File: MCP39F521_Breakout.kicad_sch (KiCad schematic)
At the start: 37 parts, among them J11 Conn_01x10, J2 Conn_01x01, J4 Conn_01x01, J5 Conn_01x01, U1 MCP39F521, U2 MCP9700AT-ETT, Y1 Crystal

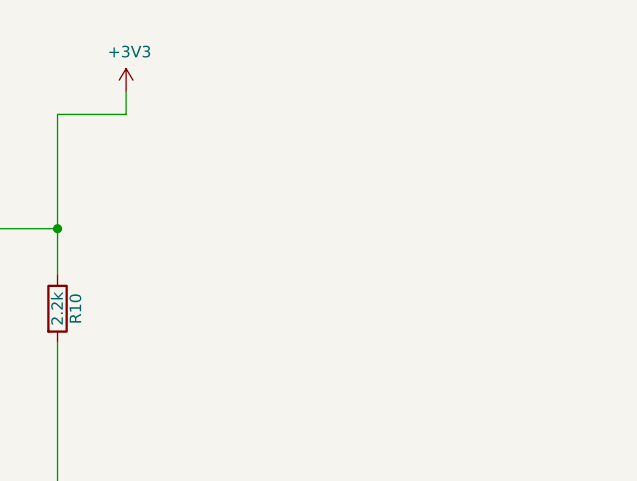
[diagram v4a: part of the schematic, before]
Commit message: Clean up silk screen
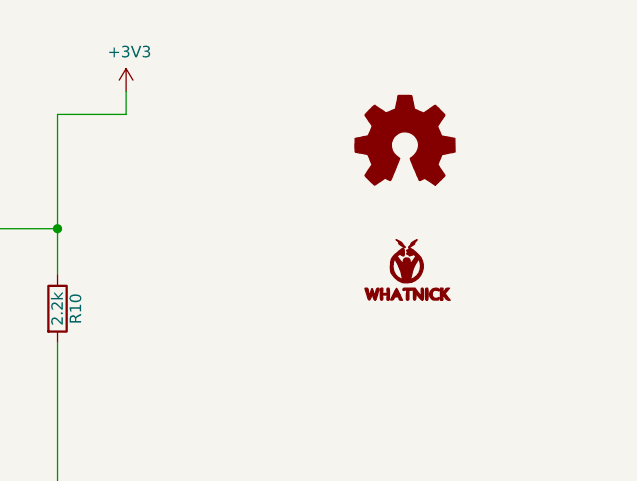
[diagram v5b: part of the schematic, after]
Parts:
- added LOGO1: Logo_Open_Hardware_Small, Symbol:OSHW-Logo2_7.3x6mm_SilkScreen, symbol Graphic:Logo_Open_Hardware_Small
- added LOGO2: LOGO, Whatnick_logo:Whatnick_logo, symbol whatnick:LOGO
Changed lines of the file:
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@@
+    )
+  )
+  (symbol (lib_id "whatnick:LOGO") (at 249.8344 59.182 0) (unit 1)
+    (in_bom yes) (on_board yes)
+    (property "Reference" "LOGO2" (id 0) (at 249.8344 61.7728 0)
+      (effects (font (size 1.524 1.524)) hide)
+    )
+    (property "Value" "LOGO" (id 1) (at 249.8344 56.5912 0)
+      (effects (font (size 1.524 1.524)) hide)
+    )
+    (property "Footprint" "Whatnick_logo:Whatnick_logo" (id 2) (at 249.8344 59.182 0)
+      (effects (font (size 1.27 1.27)) hide)
+    )
+    (property "Datasheet" "" (id 3) (at 249.8344 59.182 0)
+      (effects (font (size 1.27 1.27)) hide)
+    )
+    (property "DNP" "..." (id 4) (at 249.8344 59.182 0)
+      (effects (font (size 1.27 1.27)) hide)
+    )
+  )
+  (symbol (lib_id "Graphic:Logo_Open_Hardware_Small") (at 249.5804 45.4152 0) (unit 1)
+    (in_bom yes) (on_board yes)
+    (property "Reference" "LOGO1" (id 0) (at 249.5804 38.4302 0)
+      (effects (font (size 1.27 1.27)) hide)
+    )
+    (property "Value" "Logo_Open_Hardware_Small" (id 1) (at 249.5804 51.1302 0)
+      (effects (font (size 1.27 1.27)) hide)
+    )
+    (property "Footprint" "Symbol:OSHW-Logo2_7.3x6mm_SilkScreen" (id 2) (at 249.5804 45.4152 0)
+      (effects (font (size 1.27 1.27)) hide)
+    )
+    (property "Datasheet" "~" (id 3) (at 249.5804 45.4152 0)
+      (effects (font (size 1.27 1.27)) hide)
+    )
+    (property "DNP" "..." (id 4) (at 249.5804 45.4152 0)
+      (effects (font (size 1.27 1.27)) hide)
     )
   )
@@
       (reference "L2") (unit 1) (value "FB 300ohm") (footprint "Inductor_SMD:L_0603_1608Metric")
     )
+    (path "/ebd4b0ad-a9ba-4337-bd8b-dba09d2c6b78"
+      (reference "LOGO1") (unit 1) (value "Logo_Open_Hardware_Small") (footprint "Symbol:OSHW-Logo2_7.3x6mm_SilkScreen")
+    )
+    (path "/371039ab-54b3-4110-96fc-8866fad4e8dd"
+      (reference "LOGO2") (unit 1) (value "LOGO") (footprint "Whatnick_logo:Whatnick_logo")
+    )
     (path "/2342108e-64ef-42af-a750-f275372ffd41"

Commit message: Create gerbers and swap to non-via footprint
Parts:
- U1: footprint Package_DFN_QFN:QFN-28-1EP_5x5mm_P0.5mm_EP3.35x3.35mm_ThermalVias -> Package_DFN_QFN:QFN-28-1EP_5x5mm_P0.5mm_EP3.35x3.35mm
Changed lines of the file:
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@@
       (effects (font (size 1.524 1.524)))
     )
-    (property "Footprint" "Package_DFN_QFN:QFN-28-1EP_5x5mm_P0.5mm_EP3.35x3.35mm_ThermalVias" (id 2) (at 153.8224 74.93 0)
+    (property "Footprint" "Package_DFN_QFN:QFN-28-1EP_5x5mm_P0.5mm_EP3.35x3.35mm" (id 2) (at 153.8224 74.93 0)
       (effects (font (size 1.524 1.524)) hide)
     )
@@
     )
     (path "/da78d0ed-192f-4411-a0f9-79bdfc0c146d"
-      (reference "U1") (unit 1) (value "MCP39F521") (footprint "Package_DFN_QFN:QFN-28-1EP_5x5mm_P0.5mm_EP3.35x3.35mm_ThermalVias")
+      (reference "U1") (unit 1) (value "MCP39F521") (footprint "Package_DFN_QFN:QFN-28-1EP_5x5mm_P0.5mm_EP3.35x3.35mm")
     )
     (path "/3119c087-44b1-40ae-b65a-35145a036b16"

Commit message: Updated BOM
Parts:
- A0, A1, J2, J4, J5, TP1, TP2, TP3: DNP (none) -> ...
- C1, C2, C3, C4: manf# (none) -> 0603YC333KAT2A
- C10, C9: manf# (none) -> C0603C220K4GACTU
- C11, C5, C8: manf# (none) -> C0603C104K4PACTU
- C6, C7: manf# (none) -> CL21A225KAFNNNE
- L1, L2: manf# (none) -> NFZ2MSD301SZ10L
- R1, R2, R3, R4: manf# (none) -> CR0603-FX-1501ELF
- R10, R9: manf# (none) -> CR0603-JW-222ELF
- R11, R12: manf# (none) -> CRL0603-FW-2R40ELF
- R5, R8: manf# (none) -> CR0603-JW-472ELF
- R6: manf# (none) -> CR0603AJ/-000EAS
- R7: manf# (none) -> CR0603-FX-10R0ELF
- U1: manf# (none) -> MCP39F521-E/MQ
- U2: manf# (none) -> MCP9700T-E/TT
- Y1: manf# (none) -> LFXTAL003071Reel
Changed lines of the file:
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@@
+      (effects (font (size 1.27 1.27)) hide)
+    )
+    (property "DNP" "..." (id 4) (at 101.7524 54.61 0)
       (effects (font (size 1.27 1.27)) hide)
     )
@@
       (effects (font (size 1.27 1.27)) hide)
     )
+    (property "DNP" "..." (id 4) (at 136.0424 39.37 0)
+      (effects (font (size 1.27 1.27)) hide)
+    )
   )
   (symbol (lib_id "Connector:TestPoint") (at 160.1724 39.37 0) (unit 1)
@@
       (effects (font (size 1.27 1.27)) hide)
     )
+    (property "DNP" "..." (id 4) (at 160.1724 39.37 0)
+      (effects (font (size 1.27 1.27)) hide)
+    )
   )
   (symbol (lib_id "power:+3.3VA") (at 78.1812 131.7244 0) (unit 1)
@@
       (effects (font (size 1.27 1.27)) hide)
     )
+    (property "manf#" "CR0603-FX-1501ELF" (id 4) (at 76.3524 168.91 0)
+      (effects (font (size 1.27 1.27)) hide)
+    )
   )
   (symbol (lib_id "Device:R") (at 76.3524 180.34 0) (unit 1)
@@
       (effects (font (size 1.27 1.27)) hide)
     )
+    (property "manf#" "CR0603-FX-1501ELF" (id 4) (at 76.3524 180.34 0)
+      (effects (font (size 1.27 1.27)) hide)
+    )
   )
   (symbol (lib_id "Device:R") (at 77.978 113.9952 0) (unit 1)
@@
       (effects (font (size 1.27 1.27)) hide)
     )
+    (property "manf#" "CRL0603-FW-2R40ELF" (id 4) (at 77.978 113.9952 0)
+      (effects (font (size 1.27 1.27)) hide)
+    )
   )
   (symbol (lib_id "Device:R") (at 78.0288 94.3356 0) (unit 1)
@@
       (effects (font (size 1.27 1.27)) hide)
     )
+    (property "manf#" "CRL0603-FW-2R40ELF" (id 4) (at 78.0288 94.3356 0)
+      (effects (font (size 1.27 1.27)) hide)
+    )
   )
   (symbol (lib_id "Device:R") (at 104.2924 99.06 270) (unit 1)
@@
       (effects (font (size 1.27 1.27)) hide)
     )
+    (property "manf#" "CR0603-FX-1501ELF" (id 4) (at 104.2924 99.06 0)
+      (effects (font (size 1.27 1.27)) hide)
+    )
   )
   (symbol (lib_id "Device:R") (at 104.2924 109.22 270) (unit 1)
@@
       (effects (font (size 1.27 1.27)) hide)
     )
+    (property "manf#" "CR0603-FX-1501ELF" (id 4) (at 104.2924 109.22 0)
+      (effects (font (size 1.27 1.27)) hide)
+    )
   )
   (symbol (lib_id "Device:R") (at 109.3724 68.58 0) (unit 1)
@@
       (effects (font (size 1.27 1.27)) hide)
     )
+    (property "manf#" "CR0603-JW-472ELF" (id 4) (at 109.3724 68.58 0)
+      (effects (font (size 1.27 1.27)) hide)
+    )
   )
   (symbol (lib_id "Device:R") (at 147.4724 39.37 270) (unit 1)
@@
       (effects (font (size 1.27 1.27)) hide)
     )
+    (property "manf#" "CR0603AJ/-000EAS" (id 4) (at 147.4724 39.37 0)
+      (effects (font (size 1.27 1.27)) hide)
+    )
   )
   (symbol (lib_id "Device:R") (at 147.4724 54.61 270) (unit 1)
@@
       (effects (font (size 1.27 1.27)) hide)
     )
+    (property "manf#" "CR0603-FX-10R0ELF" (id 4) (at 147.4724 54.61 0)
+      (effects (font (size 1.27 1.27)) hide)
+    )
   )
   (symbol (lib_id "Device:R") (at 184.3024 142.24 0) (unit 1)
@@
       (effects (font (size 1.27 1.27)) hide)
     )
+    (property "manf#" "CR0603-JW-472ELF" (id 4) (at 184.3024 142.24 0)
+      (effects (font (size 1.27 1.27)) hide)
+    )
   )
   (symbol (lib_id "Device:R") (at 198.2724 63.5 0) (unit 1)
@@
       (effects (font (size 1.27 1.27)) hide)
     )
+    (property "manf#" "CR0603-JW-222ELF" (id 4) (at 198.2724 63.5 0)
+      (effects (font (size 1.27 1.27)) hide)
+    )
   )
   (symbol (lib_id "Device:R") (at 210.9724 63.5 0) (unit 1)
@@
       (effects (font (size 1.27 1.27)) hide)
     )
+    (property "manf#" "CR0603-JW-222ELF" (id 4) (at 210.9724 63.5 0)
+      (effects (font (size 1.27 1.27)) hide)
+    )
   )
   (symbol (lib_id "Device:C_Small") (at 113.1824 163.1696 0) (unit 1)
@@
       (effects (font (size 1.27 1.27)) hide)
     )
+    (property "manf#" "C0603C220K4GACTU" (id 4) (at 113.1824 163.1696 0)
+      (effects (font (size 1.27 1.27)) hide)
+    )
   )
   (symbol (lib_id "Device:C_Small") (at 119.888 163.322 0) (unit 1)
@@
     )
     (property "Datasheet" "~" (id 3) (at 119.888 163.322 0)
+      (effects (font (size 1.27 1.27)) hide)
+    )
+    (property "manf#" "C0603C220K4GACTU" (id 4) (at 119.888 163.322 0)
       (effects (font (size 1.27 1.27)) hide)
     )
@@
       (effects (font (size 1.27 1.27)) hide)
     )
+    (property "DNP" "..." (id 4) (at 101.7524 90.17 0)
+      (effects (font (size 1.27 1.27)) hide)
+    )
   )
   (symbol (lib_id "Connector_Generic:Conn_01x01") (at 180.4924 125.73 0) (unit 1)
@@
       (effects (font (size 1.27 1.27)) hide)
     )
+    (property "DNP" "..." (id 4) (at 180.4924 125.73 0)
+      (effects (font (size 1.27 1.27)) hide)
+    )
   )
   (symbol (lib_id "Connector_Generic:Conn_01x01") (at 181.7624 111.76 0) (unit 1)
@@
       (effects (font (size 1.27 1.27)) hide)
     )
+    (property "DNP" "..." (id 4) (at 181.7624 111.76 0)
+      (effects (font (size 1.27 1.27)) hide)
+    )
   )
   (symbol (lib_id "Device:C") (at 99.2124 168.91 0) (unit 1)
@@
       (effects (font (size 1.27 1.27)) hide)
     )
+    (property "DNP" "" (id 4) (at 99.2124 168.91 0)
+      (effects (font (size 1.27 1.27)) hide)
+    )
+    (property "manf#" "	0603YC333KAT2A" (id 4) (at 99.2124 168.91 0)
+      (effects (font (size 1.27 1.27)) hide)
+    )
   )
   (symbol (lib_id "Device:C") (at 99.2124 180.34 0) (unit 1)
@@
       (effects (font (size 1.27 1.27)) hide)
     )
+    (property "DNP" "" (id 4) (at 99.2124 180.34 0)
+      (effects (font (size 1.27 1.27)) hide)
+    )
+    (property "manf#" "	0603YC333KAT2A" (id 4) (at 99.2124 180.34 0)
+      (effects (font (size 1.27 1.27)) hide)
+    )
   )
   (symbol (lib_id "Device:C") (at 107.0864 85.2932 0) (unit 1)
@@
       (effects (font (size 1.27 1.27)) hide)
     )
+    (property "manf#" "C0603C104K4PACTU" (id 4) (at 107.0864 85.2932 0)
+      (effects (font (size 1.27 1.27)) hide)
+    )
   )
   (symbol (lib_id "Device:C") (at 114.4524 97.79 0) (unit 1)
@@
       (effects (font (size 1.27 1.27)) hide)
     )
+    (property "DNP" "" (id 4) (at 114.4524 97.79 0)
+      (effects (font (size 1.27 1.27)) hide)
+    )
+    (property "manf#" "	0603YC333KAT2A" (id 4) (at 114.4524 97.79 0)
+      (effects (font (size 1.27 1.27)) hide)
+    )
   )
   (symbol (lib_id "Device:C") (at 114.4524 109.22 0) (unit 1)
@@
       (effects (font (size 1.27 1.27)) hide)
     )
+    (property "DNP" "" (id 4) (at 114.4524 109.22 0)
+      (effects (font (size 1.27 1.27)) hide)
+    )
+    (property "manf#" "	0603YC333KAT2A" (id 4) (at 114.4524 109.22 0)
+      (effects (font (size 1.27 1.27)) hide)
+    )
   )
   (symbol (lib_id "Device:C") (at 120.8024 60.96 0) (unit 1)
@@
       (effects (font (size 1.27 1.27)) hide)
     )
+    (property "manf#" "C0603C104K4PACTU" (id 4) (at 120.8024 60.96 0)
+      (effects (font (size 1.27 1.27)) hide)
+    )
   )
   (symbol (lib_id "Device:C") (at 134.7724 60.96 0) (unit 1)
@@
       (effects (font (size 1.27 1.27)) hide)
     )
+    (property "manf#" "CL21A225KAFNNNE" (id 4) (at 134.7724 60.96 0)
+      (effects (font (size 1.27 1.27)) hide)
+    )
   )
   (symbol (lib_id "Device:C") (at 157.6324 60.96 0) (unit 1)
@@
       (effects (font (size 1.27 1.27)) hide)
     )
+    (property "manf#" "CL21A225KAFNNNE" (id 4) (at 157.6324 60.96 0)
+      (effects (font (size 1.27 1.27)) hide)
+    )
   )
   (symbol (lib_id "Device:C") (at 174.1424 60.96 0) (unit 1)
@@
     )
     (property "Datasheet" "" (id 3) (at 174.1424 60.96 0)
+      (effects (font (size 1.27 1.27)) hide)
+    )
+    (property "manf#" "C0603C104K4PACTU" (id 4) (at 174.1424 60.96 0)
       (effects (font (size 1.27 1.27)) hide)
     )
@@
       (effects (font (size 1.27 1.27)) hide)
     )
+    (property "manf#" "LFXTAL003071Reel" (id 4) (at 116.4336 153.7208 0)
+      (effects (font (size 1.27 1.27)) hide)
+    )
   )
   (symbol (lib_id "Device:Ferrite_Bead") (at 85.2424 99.06 270) (unit 1)
@@
       (effects (font (size 1.27 1.27)) hide)
     )
+    (property "manf#" "NFZ2MSD301SZ10L" (id 4) (at 85.2424 99.06 0)
+      (effects (font (size 1.27 1.27)) hide)
+    )
   )
   (symbol (lib_id "Device:Ferrite_Bead") (at 85.2424 109.22 270) (unit 1)
@@
       (effects (font (size 1.27 1.27)) hide)
     )
+    (property "manf#" "NFZ2MSD301SZ10L" (id 4) (at 85.2424 109.22 0)
+      (effects (font (size 1.27 1.27)) hide)
+    )
   )
   (symbol (lib_id "Jumper:SolderJumper_3_Bridged12") (at 250.7996 139.2936 0) (unit 1)
@@
       (effects (font (size 1.27 1.27)) hide)
     )
+    (property "DNP" "..." (id 4) (at 250.7996 139.2936 0)
+      (effects (font (size 1.27 1.27)) hide)
+    )
   )
   (symbol (lib_id "Jumper:SolderJumper_3_Bridged12") (at 251.0536 157.6832 0) (unit 1)
@@
       (effects (font (size 1.27 1.27)) hide)
     )
+    (property "DNP" "..." (id 4) (at 251.0536 157.6832 0)
+      (effects (font (size 1.27 1.27)) hide)
+    )
   )
   (symbol (lib_id "whatnick:LOGO") (at 249.8344 59.182 0) (unit 1)
@@
       (effects (font (size 1.27 1.27)) hide)
     )
+    (property "manf#" "MCP9700T-E/TT" (id 4) (at 78.1812 139.3444 0)
+      (effects (font (size 1.27 1.27)) hide)
+    )
   )
   (symbol (lib_id "mcp39f521:MCP39F521") (at 146.2024 124.46 0) (unit 1)
@@
       (effects (font (size 1.524 1.524)) hide)
     )
-  )
+    (property "manf#" "MCP39F521-E/MQ" (id 4) (at 146.2024 124.46 0)
+      (effects (font (size 1.27 1.27)) hide)
+    )
+  )

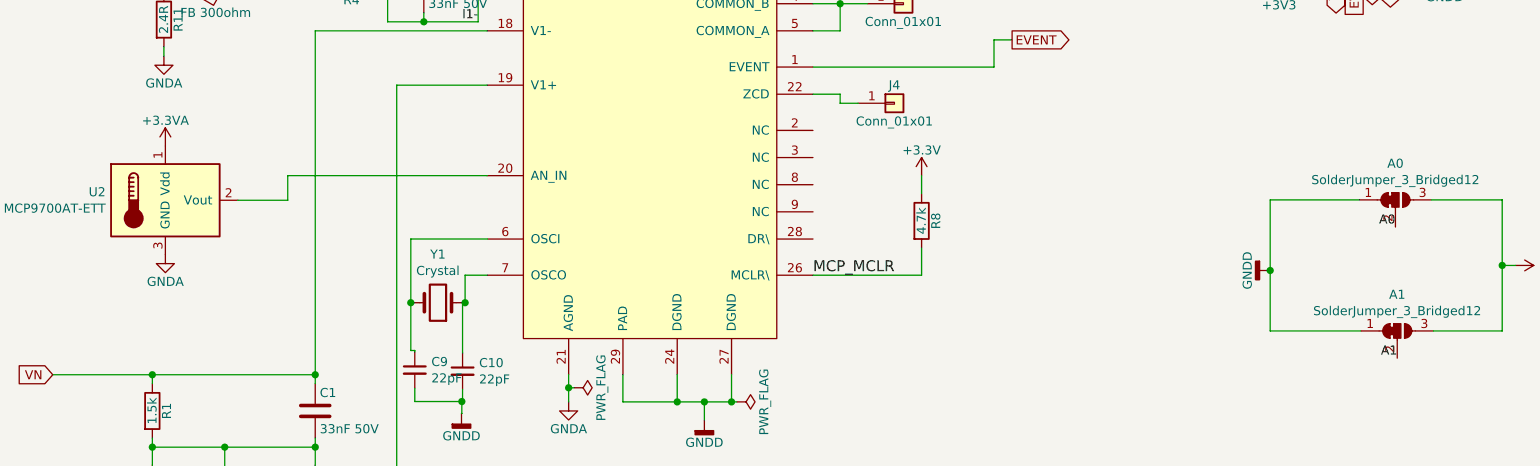
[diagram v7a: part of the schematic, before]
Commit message: Update to v7 and add elecrow BOM
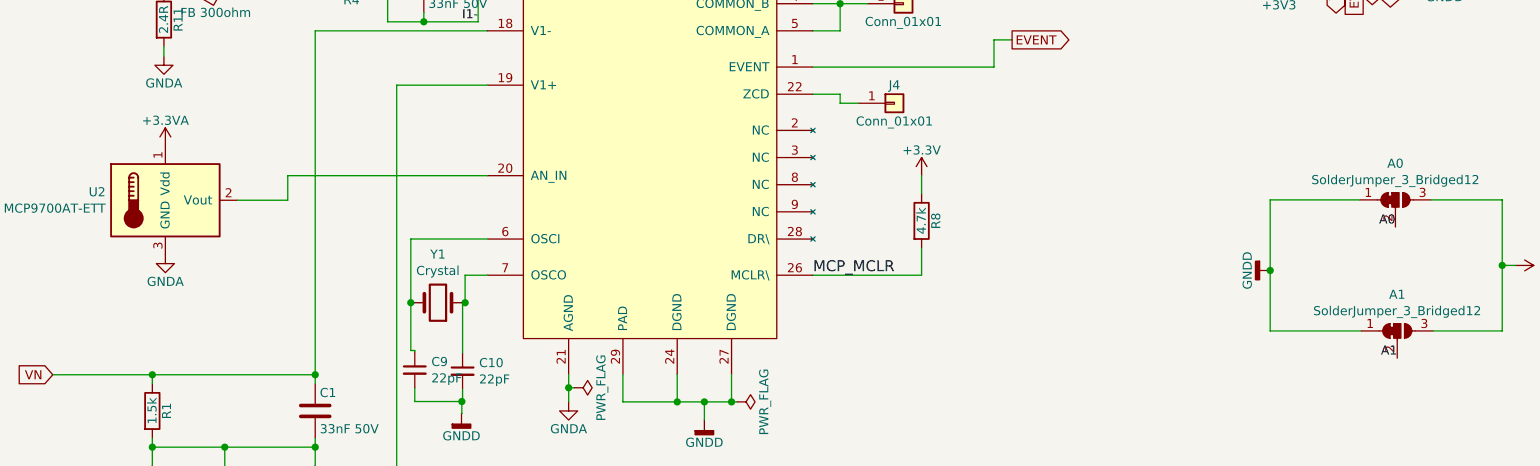
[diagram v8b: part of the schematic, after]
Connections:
- net ~RESET renamed ~{RESET}
